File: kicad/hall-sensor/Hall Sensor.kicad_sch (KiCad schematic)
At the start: 4 parts, among them J8701 ZX-SH1_0-3PLT, U8701 CC6201ST

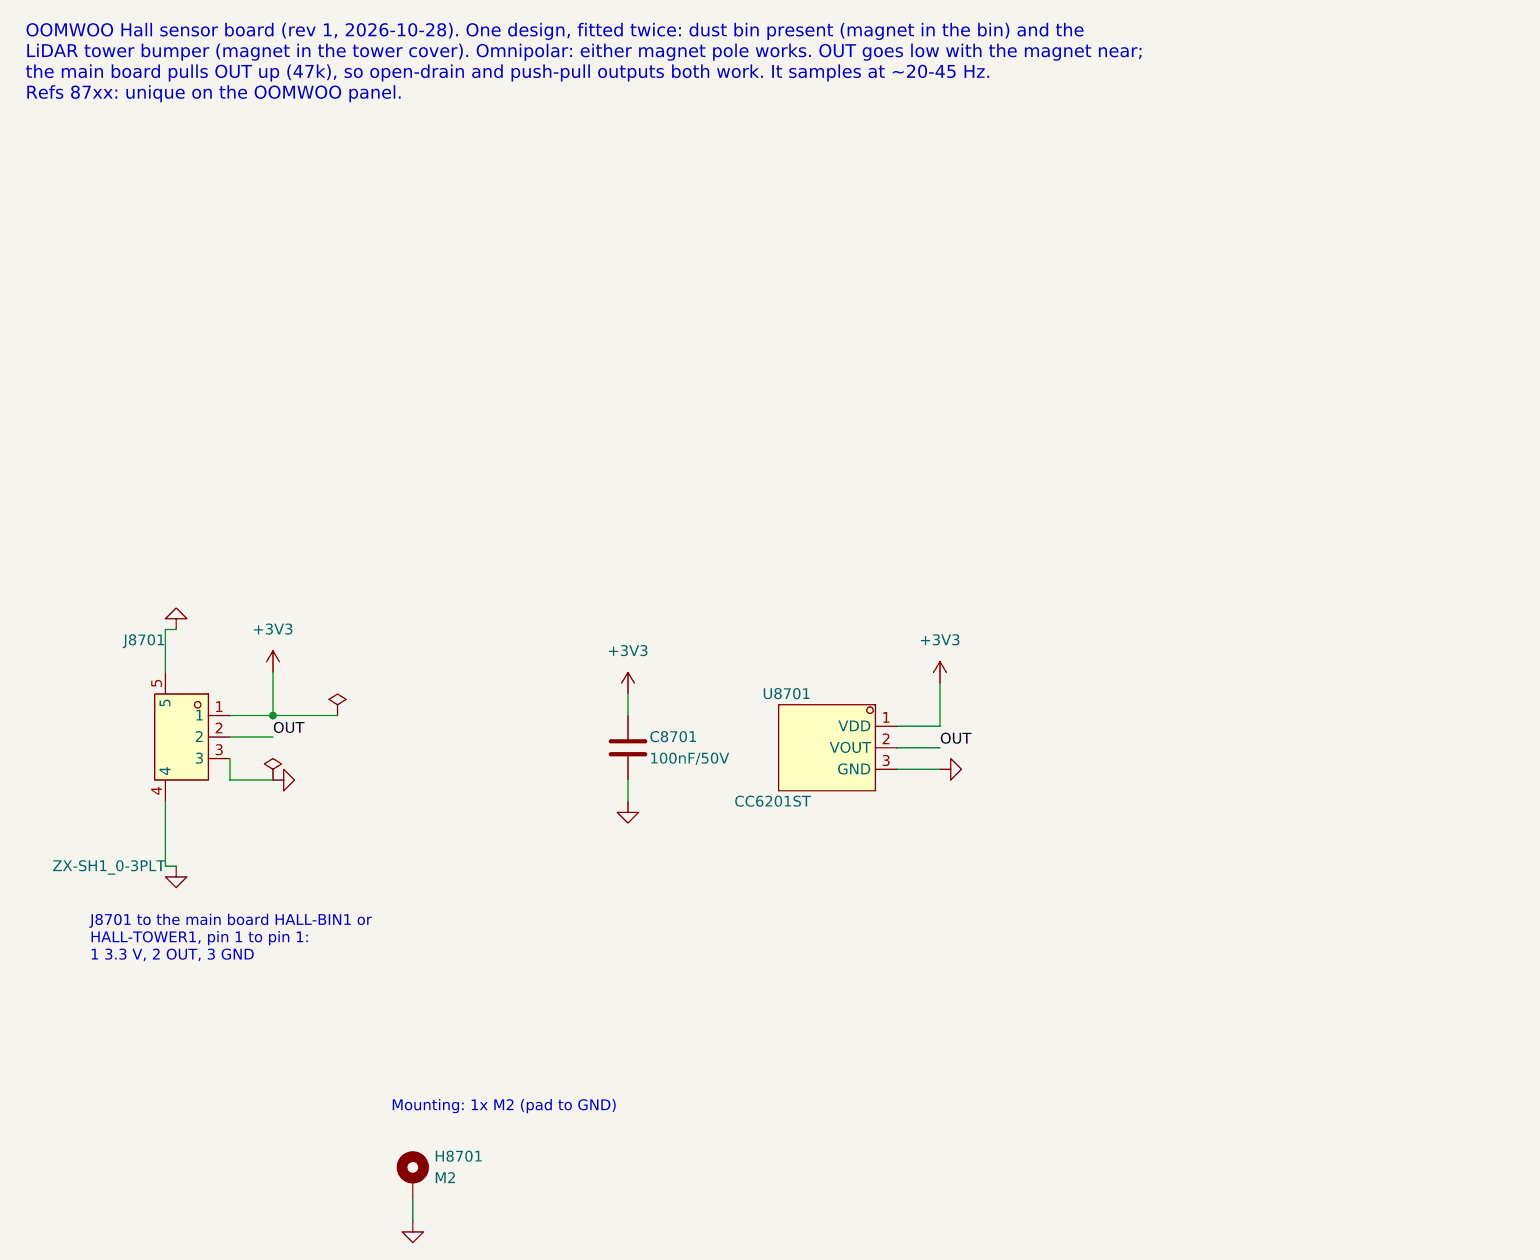
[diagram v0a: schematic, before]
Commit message: Per-board reference ranges, J1 spare header, IMU AD0 pull-down, BOM outputs
- reference ranges: main-phone 1-999, dock 1000s, front ToF 2000s, side 3000s,
  cliff 4000s, rear IR 5000s, Hall 6000s (main-phone 7xxx parts renumbered
  below 1000; sensor boards and dock moved from 8xxx)
- main-phone: J7301 -> J1, a fitted 2x7 0.1" header with spares only
  (3.3 V, 5 V, I2C4, UART PC10/PC11, PA8-PA10, PD4, PE2, PE6, GND)
- IMU: AP_AD0 pulled low by R217 (address 0x68); INT2 on test pad TP1;
  FSYNC reachable on R211; R18/R72 removed
- tools/export.py replaces export_pdfs.py: schematic PDF and JLC-style BOM in
  each board's output/ folder; --pcb adds Gerbers, placement and STEP
- cliff and rear IR projects: fix top-level sheet left over from a copy
- Hall board: visual tidy-up

Co-Authored-By: Claude Opus 5.5 <noreply@anthropic.com>
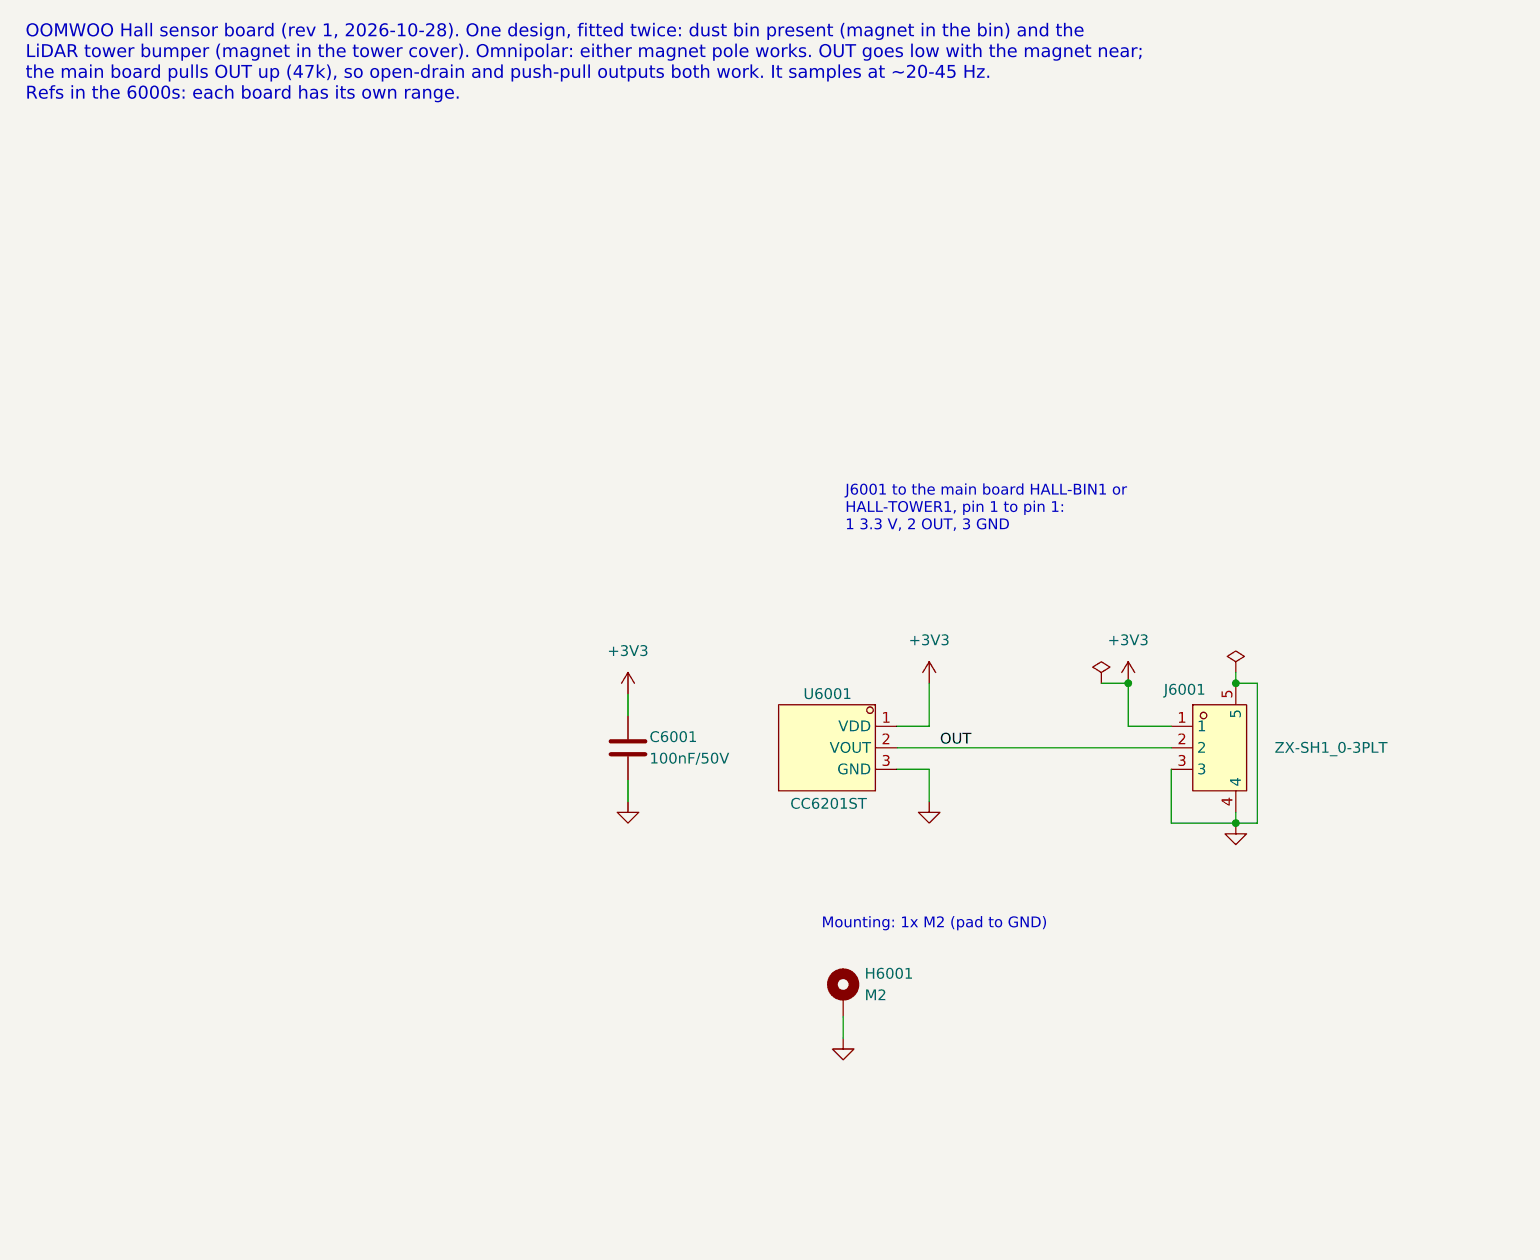
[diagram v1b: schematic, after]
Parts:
- renumbered C8701 to C6001, H8701 to H6001, J8701 to J6001, U8701 to U6001
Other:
- note added: "J6001 to the main board HALL-BIN1 or HALL-TOWER1, pin 1 to pin 1: 1 3.3 V, 2 OUT, 3 GND"
- note added: "OOMWOO Hall sensor board (rev 1, 2026-10-28). One design, fitted twice: dust bin present (magnet in the bin) and the LiDAR tower bumper (magnet in the tower cover). Omnipolar: either magnet pole works. OUT goes low with the magnet near; the main board pulls OUT up (47k), so open-drain and push-pull outputs both work. It samples at ~20-45 Hz. Refs in the 6000s: each board has its own range."
- note removed: "J8701 to the main board HALL-BIN1 or HALL-TOWER1, pin 1 to pin 1: 1 3.3 V, 2 OUT, 3 GND"
- note removed: "OOMWOO Hall sensor board (rev 1, 2026-10-28). One design, fitted twice: dust bin present (magnet in the bin) and the LiDAR tower bumper (magnet in the tower cover). Omnipolar: either magnet pole works. OUT goes low with the magnet near; the main board pulls OUT up (47k), so open-drain and push-pull outputs both work. It samples at ~20-45 Hz. Refs 87xx: unique on the OOMWOO panel."
- moved on the sheet: H6001, J6001
